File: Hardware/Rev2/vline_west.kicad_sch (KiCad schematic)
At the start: 294 parts, among them U1 AW20216S, U2 AW20216S, U3 AW20216S

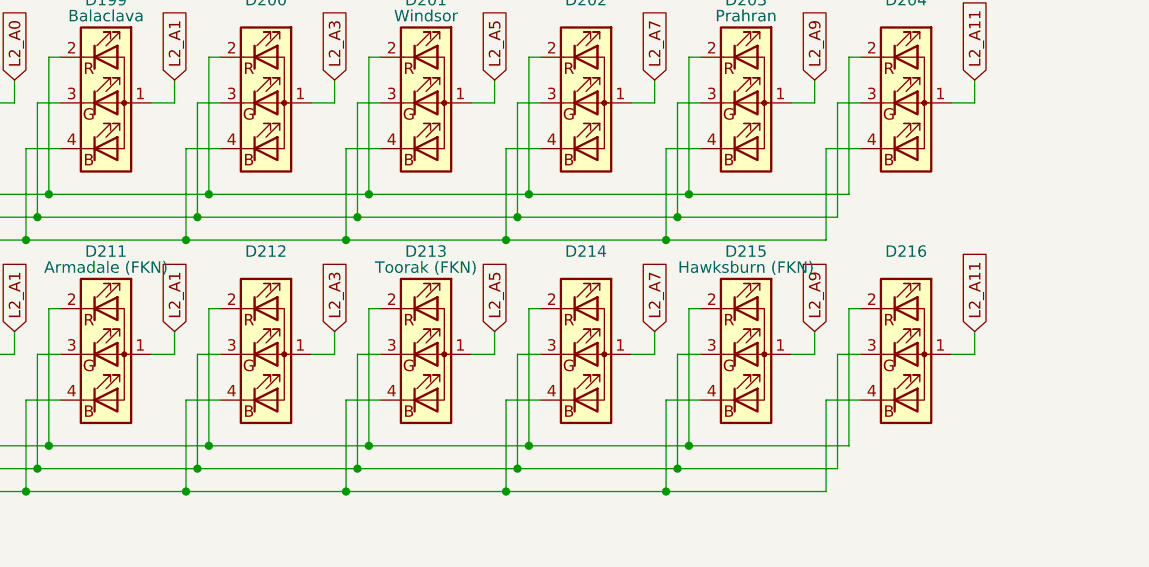
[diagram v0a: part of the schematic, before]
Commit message: fix Armadale, Toorak and Hawksburn (Frankston line) LED wiring, and add Northern group LED offsets
will need to run bodge wires for 1st batch boards
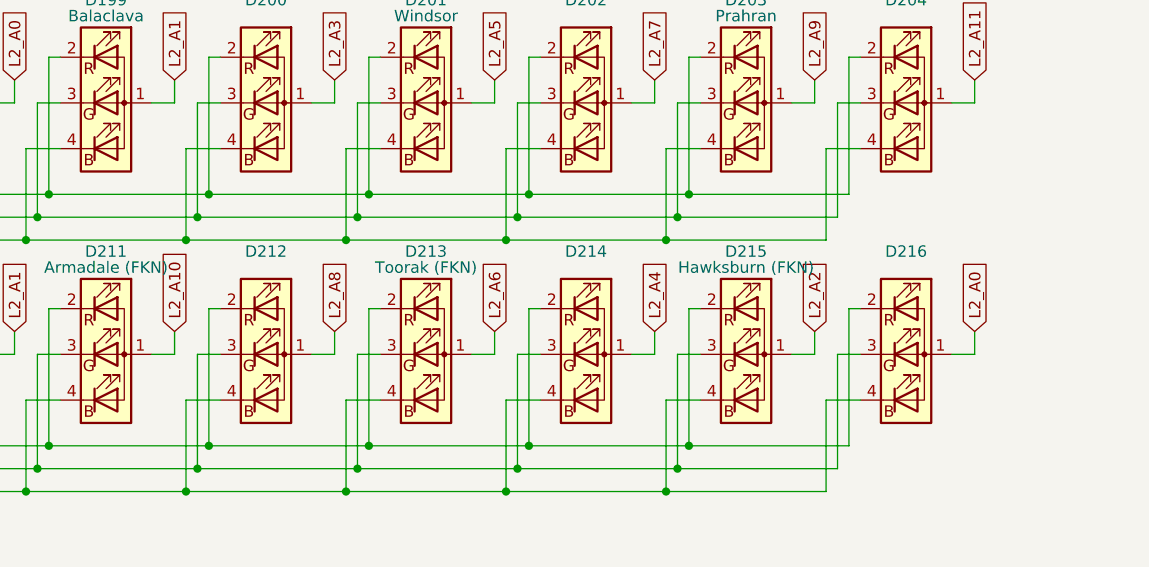
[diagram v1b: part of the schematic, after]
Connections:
- net L2_A0: now also D216.1 (A)
- net L2_A1: no longer D211.1 (A)
- net L2_A10: now also D211.1 (A)
- net L2_A11: no longer D216.1 (A)
- net L2_A2: now also D215.1 (A)
- net L2_A3: no longer D212.1 (A)
- net L2_A4: now also D214.1 (A)
- net L2_A5: no longer D213.1 (A)
- net L2_A6: now also D213.1 (A)
- net L2_A7: no longer D214.1 (A)
- net L2_A8: now also D212.1 (A)
- net L2_A9: no longer D215.1 (A)
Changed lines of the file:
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@@
 		)
 	)
-	(global_label "L2_A1"
+	(global_label "L2_A10"
 		(shape input)
 		(at 261.62 289.56 90)
@@
 		)
 		(property "Intersheetrefs" "${INTERSHEET_REFS}"
-			(at 261.62 281.0715 90)
+			(at 261.62 279.862 90)
 			(effects
 				(font
@@
 		)
 	)
-	(global_label "L2_A5"
+	(global_label "L2_A6"
 		(shape input)
 		(at 297.18 289.56 90)
@@
 		)
 	)
-	(global_label "L2_A11"
+	(global_label "L2_A0"
 		(shape input)
 		(at 350.52 289.56 90)
@@
 		)
 		(property "Intersheetrefs" "${INTERSHEET_REFS}"
-			(at 350.52 279.862 90)
+			(at 350.52 281.0715 90)
 			(effects
 				(font
@@
 		)
 	)
-	(global_label "L2_A3"
+	(global_label "L2_A8"
 		(shape input)
 		(at 279.4 289.56 90)
@@
 		)
 	)
-	(global_label "L2_A7"
+	(global_label "L2_A4"
 		(shape input)
 		(at 314.96 289.56 90)
@@
 		)
 	)
-	(global_label "L2_A9"
+	(global_label "L2_A2"
 		(shape input)
 		(at 332.74 289.56 90)

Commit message: rev.2c revised PCB layout, final
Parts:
- R184, R185, R186: MPN C2930231 -> C15401
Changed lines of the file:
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@@
 			)
 		)
-		(property "MPN" "C2930231"
+		(property "MPN" "C15401"
 			(at 458.47 285.75 90)
 			(effects
@@
 			)
 		)
-		(property "MPN" "C2930231"
+		(property "MPN" "C15401"
 			(at 52.07 304.8 90)
 			(effects
@@
 			)
 		)
-		(property "MPN" "C2930231"
+		(property "MPN" "C15401"
 			(at 50.8 217.17 90)
 			(effects
